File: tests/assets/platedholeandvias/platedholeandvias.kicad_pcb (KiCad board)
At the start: 2 copper layers, 31 x 12 mm, 2 parts

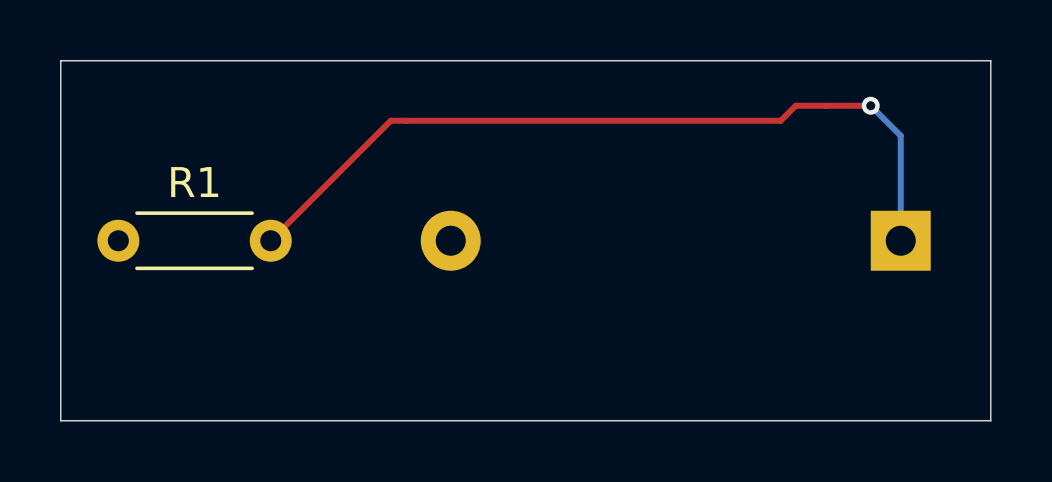
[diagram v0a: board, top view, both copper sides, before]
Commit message: fix y axis
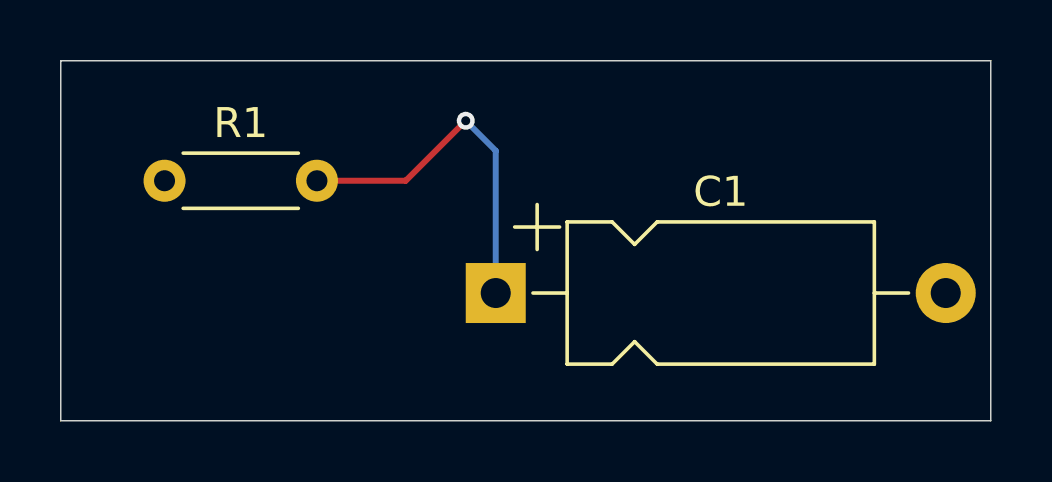
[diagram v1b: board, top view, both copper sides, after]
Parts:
- C1: moved to F.Cu
- moved C1 13.6 mm to (154.5, 106.7), turned to 0 degrees
- moved R1 2.52 mm to (143.5, 103.0)
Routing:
- net Net-(C1-Pad1): track 26.8 -> 11.9 mm
